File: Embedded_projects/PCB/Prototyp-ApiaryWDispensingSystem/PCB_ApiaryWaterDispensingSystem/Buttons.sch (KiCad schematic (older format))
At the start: 20 parts

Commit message: Many design changes have been added over the past few months #3
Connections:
- net +3V3 renamed VDD
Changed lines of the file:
@@
-	1    0    0    -1
-$EndComp
-$Comp
-L power:+3.3V #PWR?
-U 1 1 682DA7B1
-P 1880 1090
-AR Path="/67C77D26/682DA7B1" Ref="#PWR?"  Part="1"
-AR Path="/6823454A/682DA7B1" Ref="#PWR?"  Part="1"
-F 0 "#PWR?" H 1880 940 50  0001 C CNN
-F 1 "+3.3V" H 1895 1263 50  0000 C CNN
-F 2 "" H 1880 1090 50  0001 C CNN
-F 3 "" H 1880 1090 50  0001 C CNN
-	1    1880 1090
 	1    0    0    -1
 $EndComp
 Wire Wire Line
 	1880 1890 1880 1800
-Wire Wire Line
-	1880 1430 1880 1090
 Wire Wire Line
 	1680 1890 1680 1800
@@
 P 1880 2610
 AR Path="/67C77D26/682DA7BD" Ref="#PWR?"  Part="1"
-AR Path="/6823454A/682DA7BD" Ref="#PWR?"  Part="1"
-F 0 "#PWR?" H 1880 2360 50  0001 C CNN
+AR Path="/6823454A/682DA7BD" Ref="#PWR0242"  Part="1"
+F 0 "#PWR0242" H 1880 2360 50  0001 C CNN
 F 1 "GND" H 1885 2437 50  0000 C CNN
 F 2 "" H 1880 2610 50  0001 C CNN
@@
 	1    0    0    -1
 $EndComp
-$Comp
-L power:+3.3V #PWR?
-U 1 1 682DEDC2
-P 4450 1090
-AR Path="/67C77D26/682DEDC2" Ref="#PWR?"  Part="1"
-AR Path="/6823454A/682DEDC2" Ref="#PWR?"  Part="1"
-F 0 "#PWR?" H 4450 940 50  0001 C CNN
-F 1 "+3.3V" H 4465 1263 50  0000 C CNN
-F 2 "" H 4450 1090 50  0001 C CNN
-F 3 "" H 4450 1090 50  0001 C CNN
-	1    4450 1090
-	1    0    0    -1
-$EndComp
 Wire Wire Line
 	4450 1890 4450 1800
-Wire Wire Line
-	4450 1430 4450 1090
 Wire Wire Line
 	4250 1890 4250 1800
@@
 P 4450 2610
 AR Path="/67C77D26/682DEDCE" Ref="#PWR?"  Part="1"
-AR Path="/6823454A/682DEDCE" Ref="#PWR?"  Part="1"
-F 0 "#PWR?" H 4450 2360 50  0001 C CNN
+AR Path="/6823454A/682DEDCE" Ref="#PWR0244"  Part="1"
+F 0 "#PWR0244" H 4450 2360 50  0001 C CNN
 F 1 "GND" H 4455 2437 50  0000 C CNN
 F 2 "" H 4450 2610 50  0001 C CNN
@@
 	1    0    0    -1
 $EndComp
-$Comp
-L power:+3.3V #PWR?
-U 1 1 682E3092
-P 6970 1090
-AR Path="/67C77D26/682E3092" Ref="#PWR?"  Part="1"
-AR Path="/6823454A/682E3092" Ref="#PWR?"  Part="1"
-F 0 "#PWR?" H 6970 940 50  0001 C CNN
-F 1 "+3.3V" H 6985 1263 50  0000 C CNN
-F 2 "" H 6970 1090 50  0001 C CNN
-F 3 "" H 6970 1090 50  0001 C CNN
-	1    6970 1090
-	1    0    0    -1
-$EndComp
 Wire Wire Line
 	6970 1890 6970 1800
-Wire Wire Line
-	6970 1430 6970 1090
 Wire Wire Line
 	6770 1890 6770 1800
@@
 P 6970 2610
 AR Path="/67C77D26/682E309E" Ref="#PWR?"  Part="1"
-AR Path="/6823454A/682E309E" Ref="#PWR?"  Part="1"
-F 0 "#PWR?" H 6970 2360 50  0001 C CNN
+AR Path="/6823454A/682E309E" Ref="#PWR0246"  Part="1"
+F 0 "#PWR0246" H 6970 2360 50  0001 C CNN
 F 1 "GND" H 6975 2437 50  0000 C CNN
 F 2 "" H 6970 2610 50  0001 C CNN
@@
 	1    0    0    -1
 $EndComp
-$Comp
-L power:+3.3V #PWR?
-U 1 1 682E89D0
-P 9590 1090
-AR Path="/67C77D26/682E89D0" Ref="#PWR?"  Part="1"
-AR Path="/6823454A/682E89D0" Ref="#PWR?"  Part="1"
-F 0 "#PWR?" H 9590 940 50  0001 C CNN
-F 1 "+3.3V" H 9605 1263 50  0000 C CNN
-F 2 "" H 9590 1090 50  0001 C CNN
-F 3 "" H 9590 1090 50  0001 C CNN
-	1    9590 1090
-	1    0    0    -1
-$EndComp
 Wire Wire Line
 	9590 1890 9590 1800
-Wire Wire Line
-	9590 1430 9590 1090
 Wire Wire Line
 	9390 1890 9390 1800
@@
 P 9590 2610
 AR Path="/67C77D26/682E89DC" Ref="#PWR?"  Part="1"
-AR Path="/6823454A/682E89DC" Ref="#PWR?"  Part="1"
-F 0 "#PWR?" H 9590 2360 50  0001 C CNN
+AR Path="/6823454A/682E89DC" Ref="#PWR0248"  Part="1"
+F 0 "#PWR0248" H 9590 2360 50  0001 C CNN
 F 1 "GND" H 9595 2437 50  0000 C CNN
 F 2 "" H 9590 2610 50  0001 C CNN
@@
 Wire Wire Line
 	2900 1800 2820 1800
+$Comp
+L power:VDD #PWR?
+U 1 1 68F26691
+P 1880 1050
+F 0 "#PWR?" H 1880 900 50  0001 C CNN
+F 1 "VDD" H 1895 1223 50  0000 C CNN
+F 2 "" H 1880 1050 50  0001 C CNN
+F 3 "" H 1880 1050 50  0001 C CNN
+	1    1880 1050
+	1    0    0    -1
+$EndComp
+$Comp
+L power:VDD #PWR?
+U 1 1 68F27109
+P 4450 1045
+F 0 "#PWR?" H 4450 895 50  0001 C CNN
+F 1 "VDD" H 4465 1218 50  0000 C CNN
+F 2 "" H 4450 1045 50  0001 C CNN
+F 3 "" H 4450 1045 50  0001 C CNN
+	1    4450 1045
+	1    0    0    -1
+$EndComp
+$Comp
+L power:VDD #PWR?
+U 1 1 68F27C77
+P 6970 1030
+F 0 "#PWR?" H 6970 880 50  0001 C CNN
+F 1 "VDD" H 6985 1203 50  0000 C CNN
+F 2 "" H 6970 1030 50  0001 C CNN
+F 3 "" H 6970 1030 50  0001 C CNN
+	1    6970 1030
+	1    0    0    -1
+$EndComp
+$Comp
+L power:VDD #PWR?
+U 1 1 68F28670
+P 9590 1060
+F 0 "#PWR?" H 9590 910 50  0001 C CNN
+F 1 "VDD" H 9605 1233 50  0000 C CNN
+F 2 "" H 9590 1060 50  0001 C CNN
+F 3 "" H 9590 1060 50  0001 C CNN
+	1    9590 1060
+	1    0    0    -1
+$EndComp
+Wire Wire Line
+	9590 1060 9590 1430
+Wire Wire Line
+	6970 1030 6970 1430
+Wire Wire Line
+	4450 1045 4450 1430
+Wire Wire Line
+	1880 1050 1880 1430
 $EndSCHEMATC

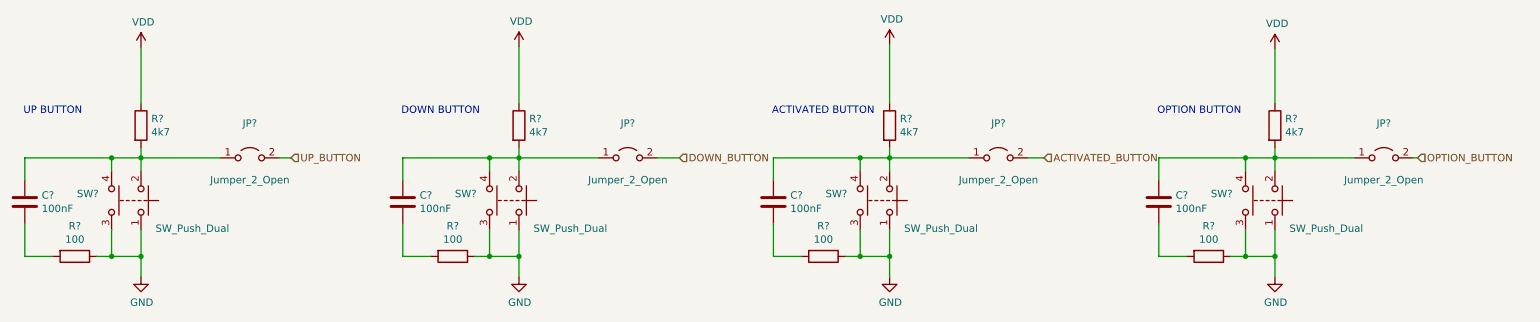
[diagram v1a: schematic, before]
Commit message: All signal has been routed, the analog part needs to be completed
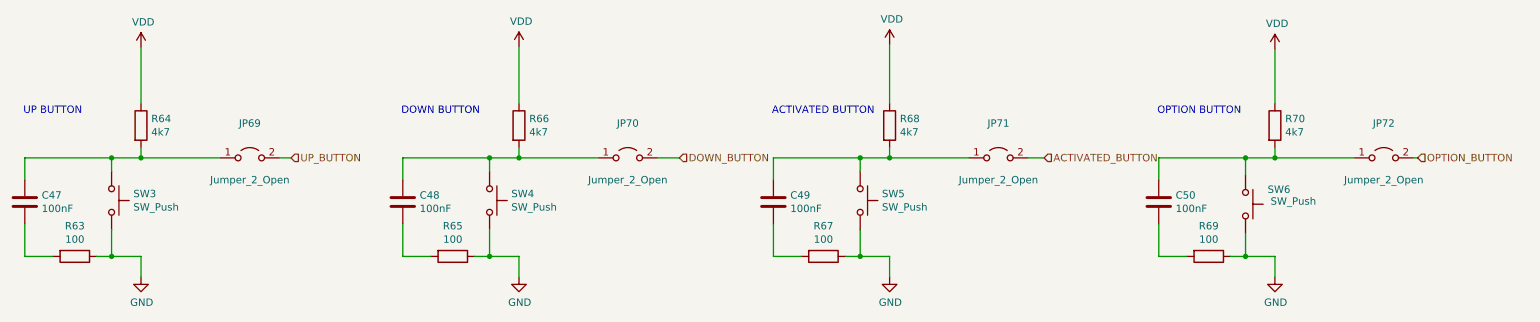
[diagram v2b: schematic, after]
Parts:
- removed SW? (x4): SW_Push_Dual, Button_Switch_SMD:SW_Push_1P1T_NO_6x6mm_H9.5mm, symbol Switch:SW_Push_Dual
- added SW3, SW4, SW5, SW6: SW_Push, Button_Switch_THT:SW_PUSH-12mm, symbol Switch:SW_Push
- C47, C48, C49, C50: renamed from C?; footprint Capacitor_SMD:C_0805_2012Metric -> Capacitor_SMD:C_0603_1608Metric
- R63, R65, R67, R69: renamed from R?; footprint Resistor_SMD:R_0805_2012Metric -> Resistor_SMD:R_0603_1608Metric
- R64, R66, R68, R70: renamed from R?; footprint (none) -> Resistor_SMD:R_0603_1608Metric
- gave numbers to parts that had none: 4
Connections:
- net GND: now also SW3.2, SW4.2, SW5.2, SW6.2
- net at C47.1, JP69.1 (A), R64.2: now also SW3.1
- net at C48.1, JP70.1 (A), R66.2: now also SW4.1
- net at C49.1, JP71.1 (A), R68.2: now also SW5.1
- net at C50.1, JP72.1 (A), R70.2: now also SW6.1
